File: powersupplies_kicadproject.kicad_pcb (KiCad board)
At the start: 6 copper layers, 160 x 99 mm, 18 parts, among them U2 TSR2-2465, U3 TSR2-2465

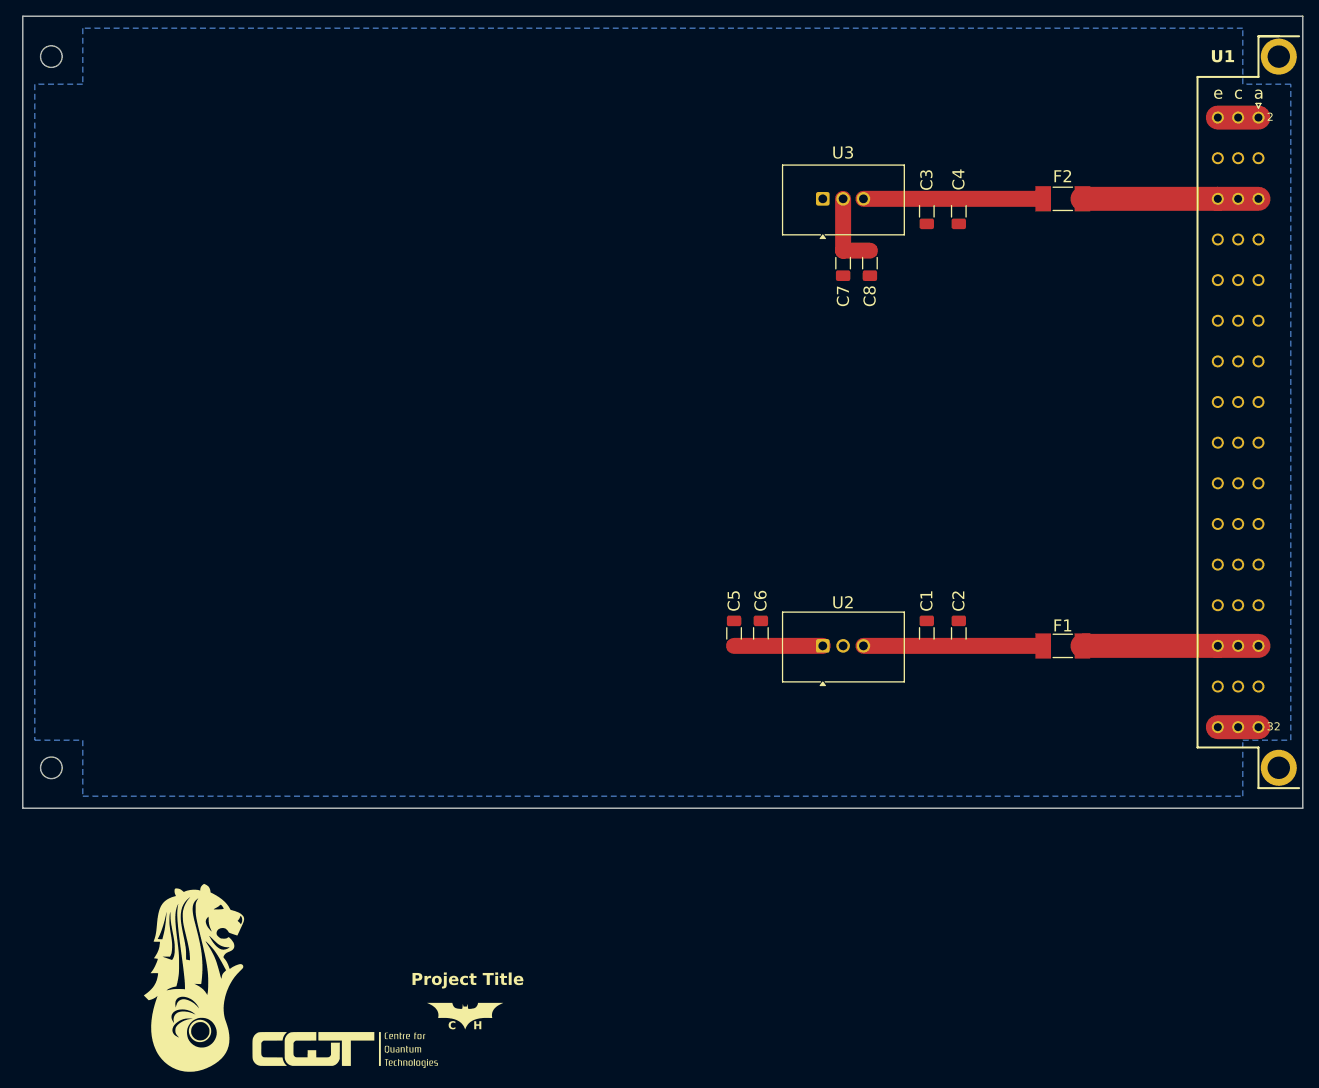
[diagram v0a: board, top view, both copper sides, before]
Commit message: Added and routed power LEDs.
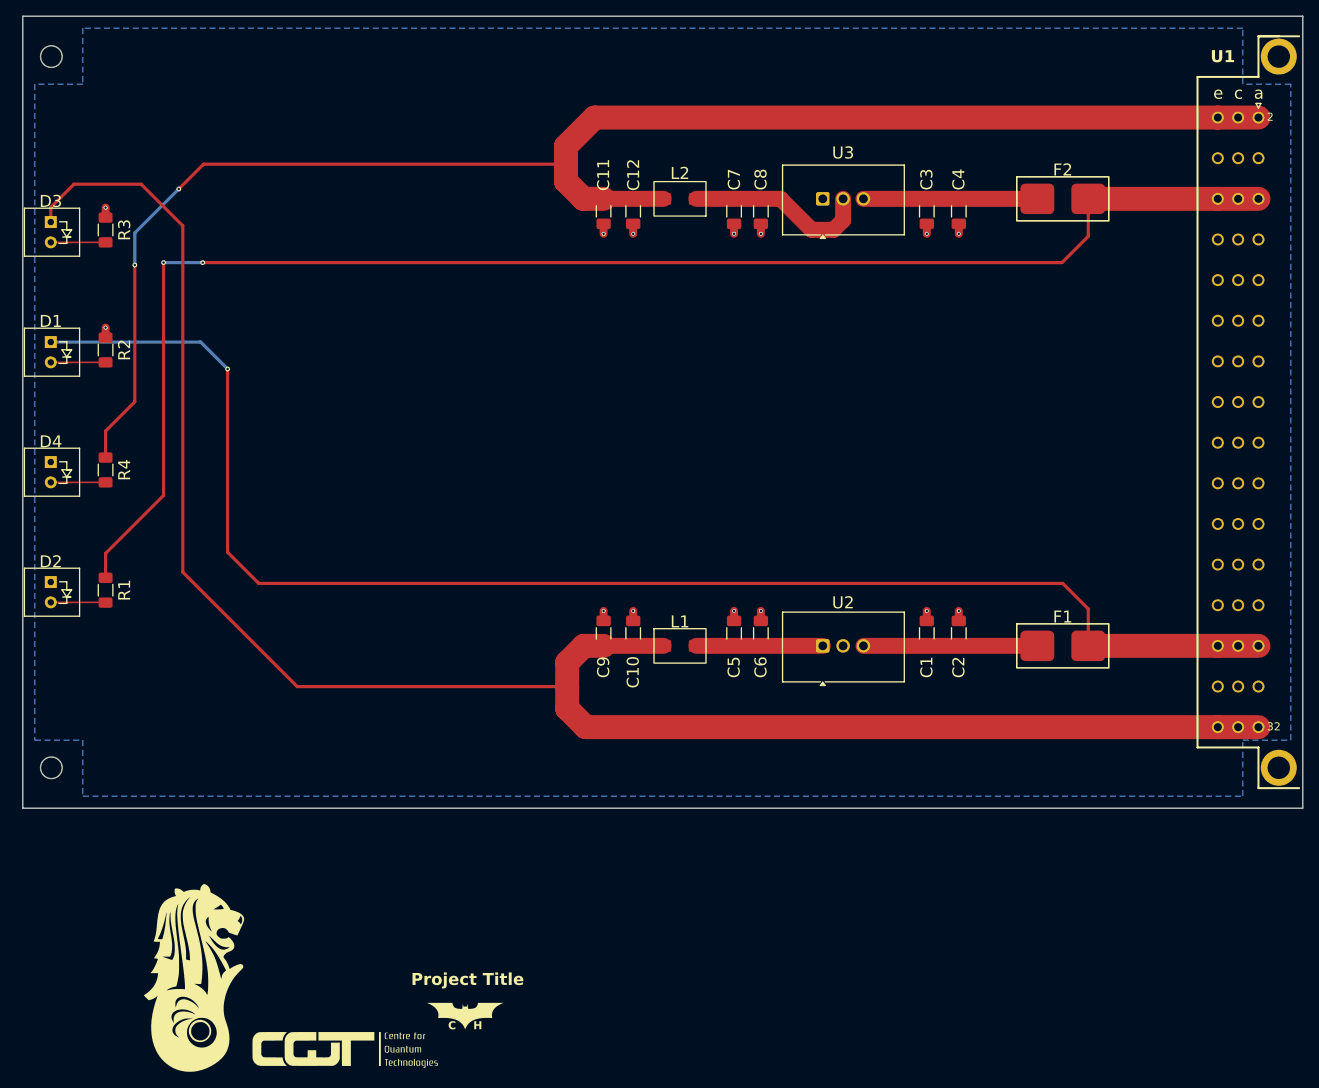
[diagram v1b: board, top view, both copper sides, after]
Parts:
- added C10: 10uF, Capacitor_SMD:C_1206_3216Metric_Pad1.33x1.80mm_HandSolder, F.Cu at (176.3, 127.6)
- added C11: 10uF, Capacitor_SMD:C_1206_3216Metric_Pad1.33x1.80mm_HandSolder, F.Cu at (172.6, 74.9)
- added C12: 10uF, Capacitor_SMD:C_1206_3216Metric_Pad1.33x1.80mm_HandSolder, F.Cu at (176.3, 74.9)
- added C9: 10uF, Capacitor_SMD:C_1206_3216Metric_Pad1.33x1.80mm_HandSolder, F.Cu at (172.6, 127.6)
- added D1: LED_Green, 1_LED_TH:LED_TH_RA, F.Cu at (103.5, 92.5)
- added D2: LED_Yellow, 1_LED_TH:LED_TH_RA, F.Cu at (103.5, 122.5)
- added D3: LED_Green, 1_LED_TH:LED_TH_RA, F.Cu at (103.5, 77.5)
- added D4: LED_Yellow, 1_LED_TH:LED_TH_RA, F.Cu at (103.5, 107.5)
- added L1: 5.6uH, 1_L_SMD:TCK141, F.Cu at (182.2, 129.2)
- added L2: 5.6uH, 1_L_SMD:TCK141, F.Cu at (182.2, 73.3)
- added R1: 680R, Resistor_SMD:R_1206_3216Metric_Pad1.30x1.75mm_HandSolder, F.Cu at (110.3, 122.2)
- added R2: 680R, Resistor_SMD:R_1206_3216Metric_Pad1.30x1.75mm_HandSolder, F.Cu at (110.3, 92.2)
- added R3: 680R, Resistor_SMD:R_1206_3216Metric_Pad1.30x1.75mm_HandSolder, F.Cu at (110.3, 77.2)
- added R4: 680R, Resistor_SMD:R_1206_3216Metric_Pad1.30x1.75mm_HandSolder, F.Cu at (110.3, 107.2)
- F1, F2: footprint Fuse:Fuse_Littelfuse-NANO2-451_453 -> 1_Fuse_SMD:LittleFuse_01550900M
- moved C7 15.1 mm to (188.9, 74.9)
- moved C8 15.1 mm to (192.3, 74.9)
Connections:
- C5 pad 1: /6.5V Dual Rail Power/+15V -> Net-(U2-Vin)
- C6 pad 1: /6.5V Dual Rail Power/+15V -> Net-(U2-Vin)
- C7 pad 2: /6.5V Dual Rail Power/-15V -> Net-(U3-GND)
- C8 pad 2: /6.5V Dual Rail Power/-15V -> Net-(U3-GND)
- U2 pad 1: /6.5V Dual Rail Power/+15V -> Net-(U2-Vin)
- U3 pad 2: /6.5V Dual Rail Power/-15V -> Net-(U3-GND)
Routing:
- net /6.5V Dual Rail Power/+15V: track 16.2 -> 225.0 mm
- net /6.5V Dual Rail Power/-15V: track 14.9 -> 192.6 mm, vias 0 -> 2
- net /6.5V Dual Rail Power/-6.5V: track 22.0 -> 185.3 mm, vias 0 -> 2
- net /6.5V Dual Rail Power/+6.5V: track 22.0 -> 182.8 mm, vias 0 -> 1
- net Net-(U3-GND): track 0.00 -> 23.1 mm
- net GND: track 0.00 -> 17.4 mm, vias 0 -> 14
- net Net-(U2-Vin): track 0.00 -> 15.8 mm
- net Net-(D2-K): track 0.00 -> 6.86 mm
- net Net-(D4-K): track 0.00 -> 6.85 mm
- net Net-(D3-K): track 0.00 -> 6.85 mm
- net Net-(D1-K): track 0.00 -> 6.85 mm
- removed copper zone on In2.Cu, net (none)
- removed copper zone on In4.Cu, net (none)
- removed copper zone on In1.Cu, net GND
- removed copper zone on In3.Cu, net GND
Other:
- copper layers 6 -> 2

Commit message: Added fab files.
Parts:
- moved G*** 120.1 mm to (229.1, 98.7)
- moved G*** 110.7 mm to (205.1, 98.7)
- moved G*** 32.6 mm to (159.2, 143.1)
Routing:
- net GND: vias 14 -> 130
- added copper zone on F.Cu, net GND
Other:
- board text added: "LED: +15V"
- board text added: "LED: +6.5V"
- board text added: "LED: -15V"
- board text added: "LED: -6.5V"
- board text added: "Powersupplies: design1"
- board text removed: "Project Title"
